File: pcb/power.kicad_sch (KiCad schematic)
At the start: 19 parts, among them CN3 ZX-PH2.0-WT2P, J3 GT-USB-7010ASV, Q1 DMG3415U-7, U2 RT9080-33GJ5, U3 MAX17048G+T10, U4 MCP73831-2DCI/MC

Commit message: Lots of work on schematics
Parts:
- added D2: ESDA7P60-1U1M, prop-devboard:D1610-RD, symbol prop-devboard:ESDA7P60-1U1M
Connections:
- net GND: now also D2.2
- net VBUS: now also D2.1
- net VREG_EN: now reaches R4.1, U2.3 (EN)
- net VIN: now reaches C1.2, D1.1, Q1.3, R4.2, U2.1 (VIN)
- net BAT_SCL renamed I2C3_SCL
- net BAT_SDA renamed I2C3_SDA
- no-connect marks 3 -> 10
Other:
- moved on the sheet: C2, R4, U2

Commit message: Mostly finished PCB layout
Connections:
- net GND: now also U4.9 (EP)
- no-connect marks 10 -> 11
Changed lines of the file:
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@@
+	)
+	(junction
+		(at 190.5 129.54)
+		(diameter 0)
+		(color 0 0 0 0)
 	)
 	(junction
@@
 		(at 55.88 52.07)
 	)
+	(no_connect
+		(at 187.96 127)
+	)
 	(wire
 		(pts
@@
 	(wire
 		(pts
+			(xy 190.5 129.54) (xy 203.2 129.54)
+		)
+		(stroke
+			(width 0)
+			(type default)
+		)
+	)
+	(wire
+		(pts
+			(xy 190.5 121.92) (xy 190.5 129.54)
+		)
+		(stroke
+			(width 0)
+			(type default)
+		)
+	)
+	(wire
+		(pts
 			(xy 165.1 78.74) (xy 171.45 78.74)
 		)
@@
 	(wire
 		(pts
+			(xy 187.96 121.92) (xy 190.5 121.92)
+		)
+		(stroke
+			(width 0)
+			(type default)
+		)
+	)
+	(wire
+		(pts
 			(xy 121.92 135.89) (xy 121.92 140.97)
 		)
@@
 	(wire
 		(pts
-			(xy 187.96 129.54) (xy 203.2 129.54)
-		)
-		(stroke
+			(xy 187.96 129.54) (xy 190.5 129.54)
+		)
+		(stroke

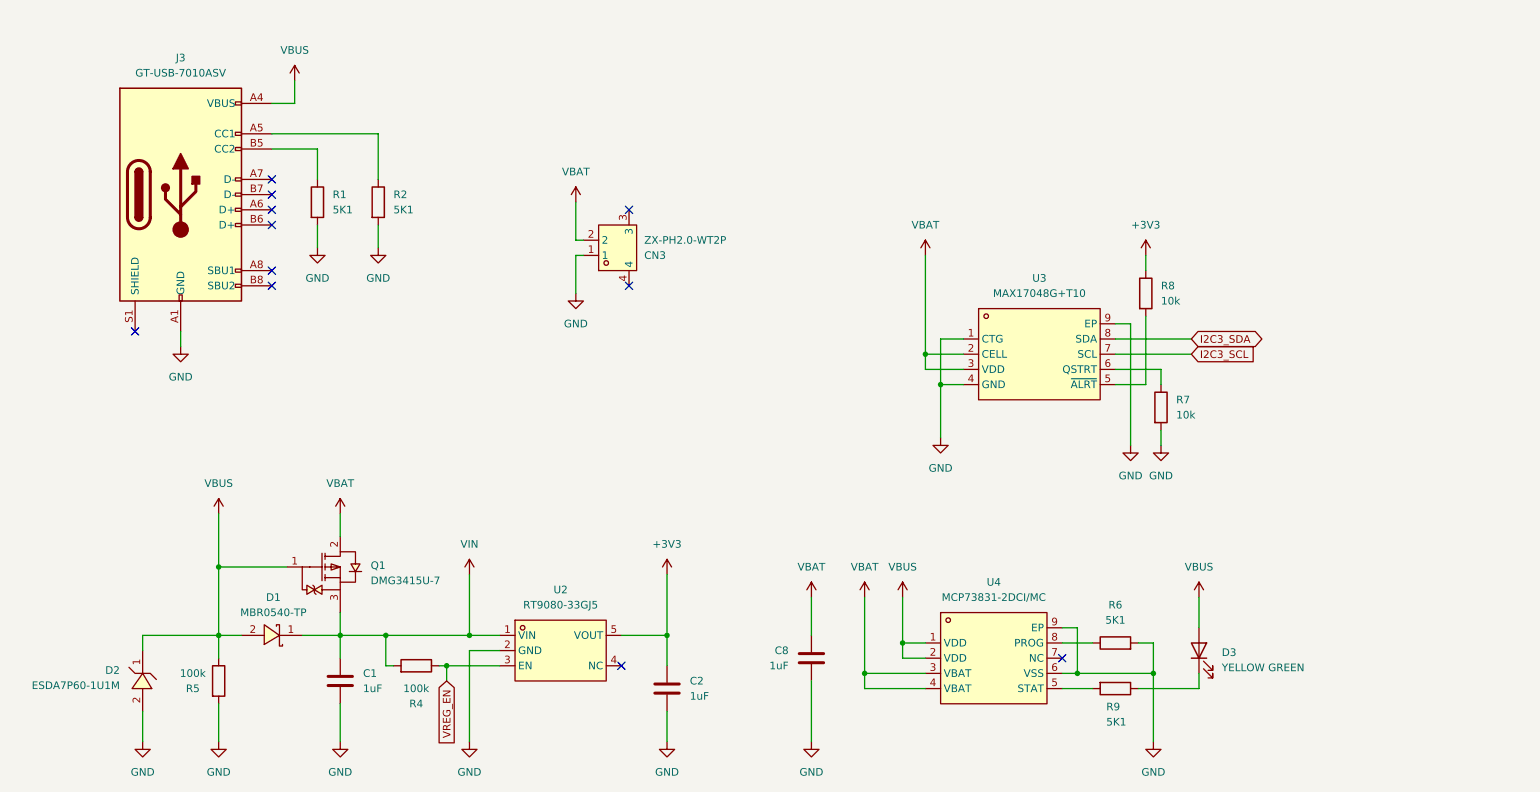
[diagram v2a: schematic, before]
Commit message: Added USB support
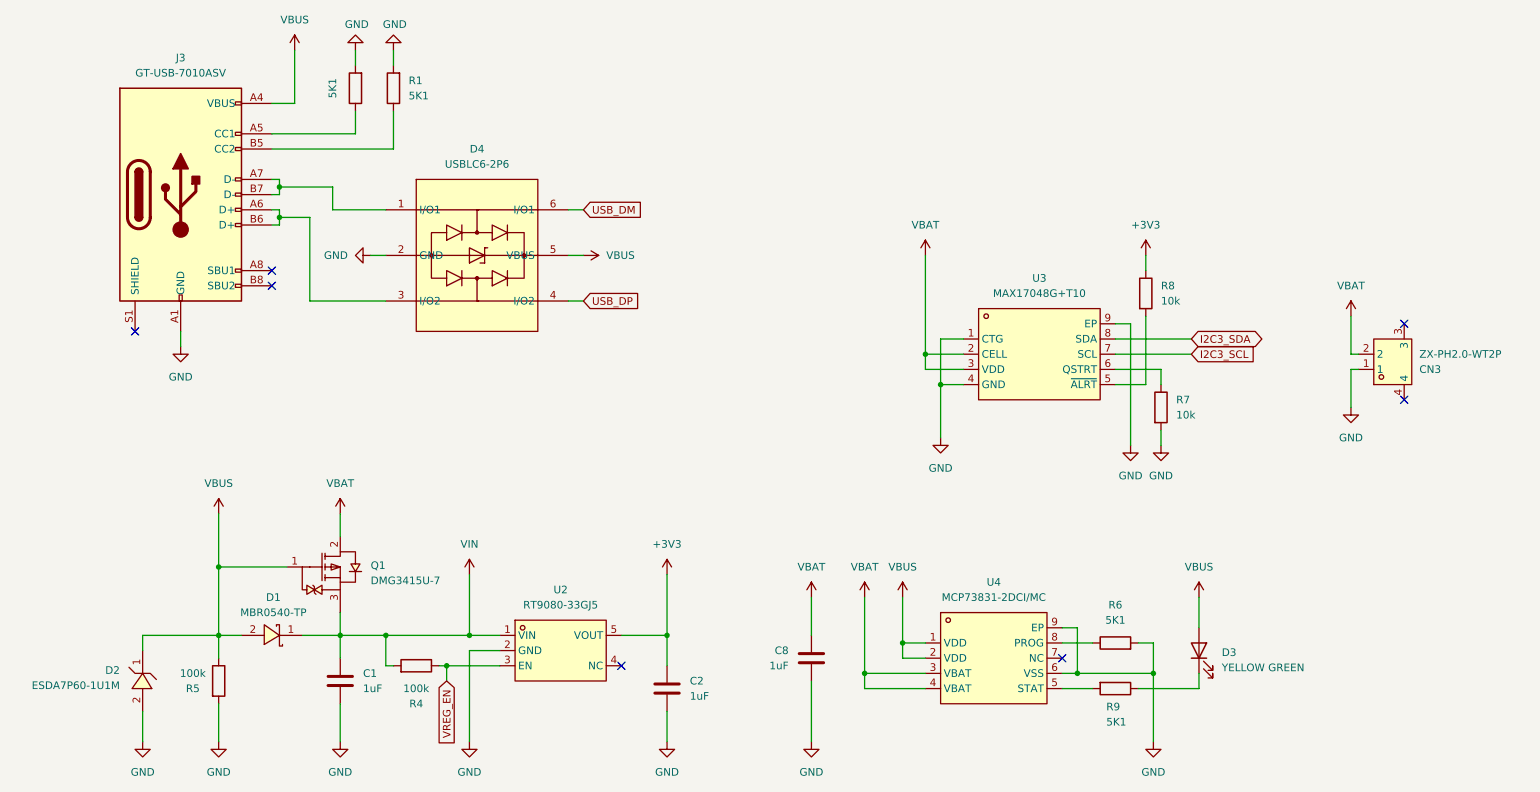
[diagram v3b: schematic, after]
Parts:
- added D4: USBLC6-2P6, prop-devboard:SOT-666-6_L1.6-W1.2-P0.50-LS1.6-BR, symbol prop-devboard:USBLC6-2P6
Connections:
- net GND: now also D4.2 (GND)
- net VBUS: now also D4.5 (VBUS)
- net at J3.A6 (D+): now also J3.B6 (D+), D4.3 (I/O2)
- net at J3.A7 (D-): now also J3.B7 (D-), D4.1 (I/O1)
- new net USB_DM: D4.6 (I/O1)
- new net USB_DP: D4.4 (I/O2)
- no-connect marks 11 -> 7
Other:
- moved on the sheet: CN3, R1

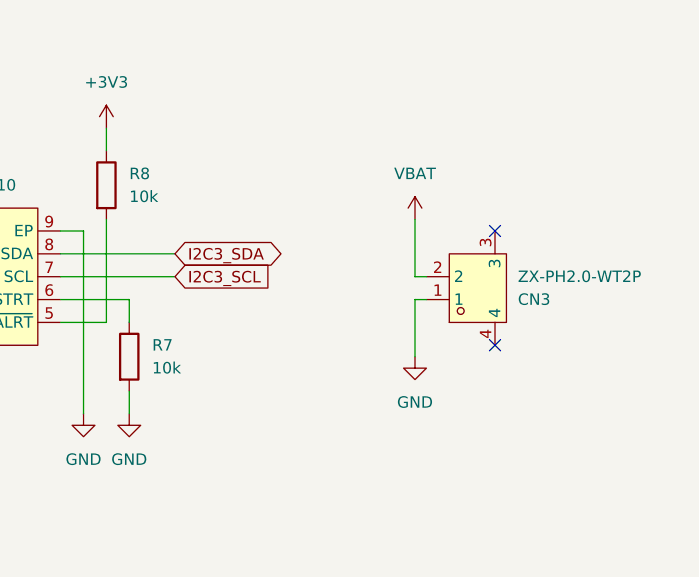
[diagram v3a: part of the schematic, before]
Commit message: Fixed wrong polarity of the battery connector, uffff
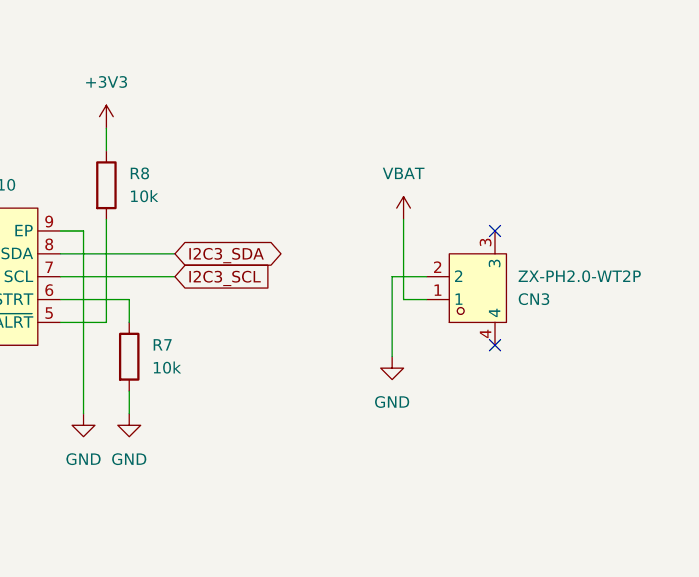
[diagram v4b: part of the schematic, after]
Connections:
- net GND: now also CN3.2; no longer CN3.1
- net VBAT: now also CN3.1; no longer CN3.2
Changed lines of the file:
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@@
 	(wire
 		(pts
-			(xy 236.22 76.2) (xy 236.22 69.85)
-		)
-		(stroke
-			(width 0)
-			(type default)
-		)
-	)
-	(wire
-		(pts
 			(xy 190.5 129.54) (xy 203.2 129.54)
 		)
@@
 	(wire
 		(pts
+			(xy 234.95 69.85) (xy 234.95 78.74)
+		)
+		(stroke
+			(width 0)
+			(type default)
+		)
+	)
+	(wire
+		(pts
 			(xy 88.9 125.73) (xy 88.9 140.97)
 		)
@@
 	(wire
 		(pts
+			(xy 234.95 78.74) (xy 237.49 78.74)
+		)
+		(stroke
+			(width 0)
+			(type default)
+		)
+	)
+	(wire
+		(pts
 			(xy 46.99 111.76) (xy 46.99 123.19)
 		)
@@
 	(wire
 		(pts
-			(xy 237.49 78.74) (xy 236.22 78.74)
-		)
-		(stroke
-			(width 0)
-			(type default)
-		)
-	)
-	(wire
-		(pts
 			(xy 146.05 116.84) (xy 146.05 123.19)
 		)
@@
 	(wire
 		(pts
-			(xy 236.22 78.74) (xy 236.22 85.09)
+			(xy 233.68 76.2) (xy 233.68 85.09)
 		)
 		(stroke
@@
 	(wire
 		(pts
+			(xy 237.49 76.2) (xy 233.68 76.2)
+		)
+		(stroke
+			(width 0)
+			(type default)
+		)
+	)
+	(wire
+		(pts
 			(xy 165.1 76.2) (xy 171.45 76.2)
 		)
@@
 	(wire
 		(pts
-			(xy 237.49 76.2) (xy 236.22 76.2)
-		)
-		(stroke
-			(width 0)
-			(type default)
-		)
-	)
-	(wire
-		(pts
 			(xy 161.29 116.84) (xy 161.29 124.46)
 		)
@@
 	(symbol
 		(lib_id "power:VBUS")
-		(at 236.22 69.85 0)
+		(at 234.95 69.85 0)
 		(unit 1)
 		(exclude_from_sim no)
@@
 		(fields_autoplaced yes)
 		(property "Reference" "#PWR017"
-			(at 236.22 73.66 0)
+			(at 234.95 73.66 0)
 			(effects
 				(font
@@
 		)
 		(property "Value" "VBAT"
-			(at 236.22 64.77 0)
+			(at 234.95 64.77 0)
 			(effects
 				(font
@@
 		)
 		(property "Footprint" ""
-			(at 236.22 69.85 0)
+			(at 234.95 69.85 0)
 			(effects
 				(font
@@
 		)
 		(property "Datasheet" ""
-			(at 236.22 69.85 0)
+			(at 234.95 69.85 0)
 			(effects
 				(font
@@
 		)
 		(property "Description" "Power symbol creates a global label with name \"VBUS\""
-			(at 236.22 69.85 0)
+			(at 234.95 69.85 0)
 			(effects
 				(font
@@
 	(symbol
 		(lib_id "power:GND")
-		(at 236.22 85.09 0)
+		(at 233.68 85.09 0)
 		(unit 1)
 		(exclude_from_sim no)
@@
 		(fields_autoplaced yes)
 		(property "Reference" "#PWR015"
-			(at 236.22 91.44 0)
+			(at 233.68 91.44 0)
 			(effects
 				(font
@@
 		)
 		(property "Value" "GND"
-			(at 236.22 90.17 0)
+			(at 233.68 90.17 0)
 			(effects
 				(font
@@
 		)
 		(property "Footprint" ""
-			(at 236.22 85.09 0)
+			(at 233.68 85.09 0)
 			(effects
 				(font
@@
 		)
 		(property "Datasheet" ""
-			(at 236.22 85.09 0)
+			(at 233.68 85.09 0)
 			(effects
 				(font
@@
 		)
 		(property "Description" "Power symbol creates a global label with name \"GND\" , ground"
-			(at 236.22 85.09 0)
+			(at 233.68 85.09 0)
 			(effects
 				(font

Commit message: Switched battery and QWIIC connectors to black ones, and fixed their positioning to not obstruct bolt heads when M2.5 cylindrical bolts are used to mount the board
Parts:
- CN3: footprint prop-devboard:CONN-SMD_ZX-PH2.0-WT2P -> prop-devboard:CONN-SMD_PH-2AWT; LCSC Part C7429689 -> C19633668
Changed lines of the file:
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@@
 			)
 		)
-		(property "Footprint" "prop-devboard:CONN-SMD_ZX-PH2.0-WT2P"
+		(property "Footprint" "prop-devboard:CONN-SMD_PH-2AWT"
 			(at 241.3 63.5 0)
 			(effects
@@
 			)
 		)
-		(property "LCSC Part" "C7429689"
+		(property "LCSC Part" "C19633668"
 			(at 241.3 60.96 0)
 			(effects
 				(font
+					(size 1.27 1.27)
+				)
+				(hide yes)
+			)
+		)
+		(property "LCSC Part #" ""
+			(at 241.3 77.47 0)
+			(effects
+				(font

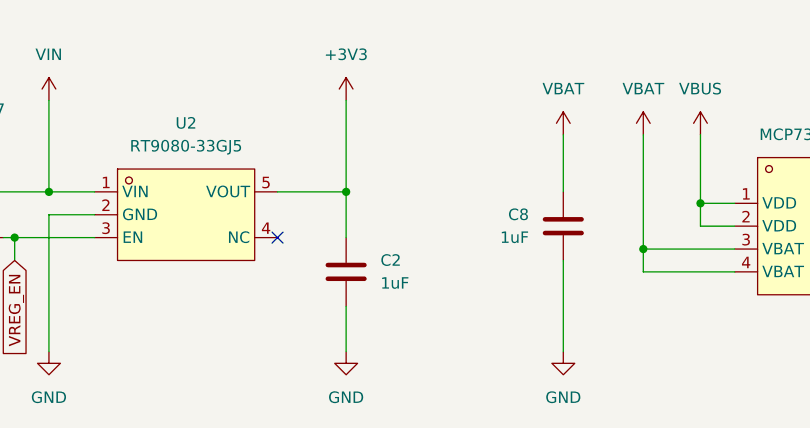
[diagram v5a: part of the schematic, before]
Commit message: Added I2C pull ups, extra bypass capacitance for the MCU and increased the LDO output capacitance
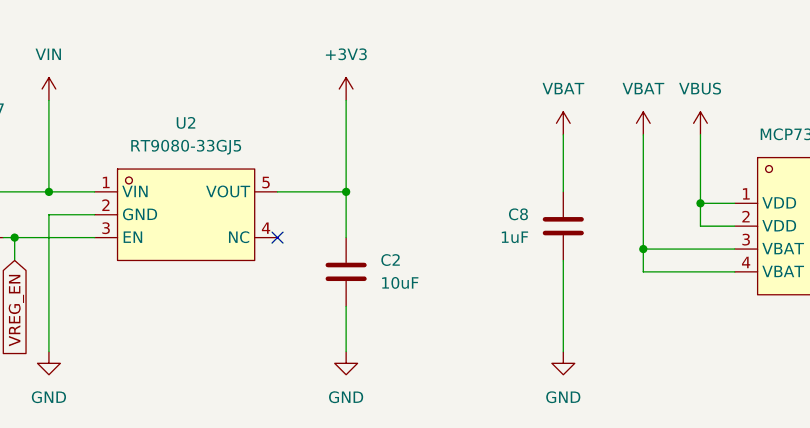
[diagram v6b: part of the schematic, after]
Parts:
- C2: value 1uF -> 10uF; LCSC Part # C14445 -> C15525
- R5: LCSC Part # C60491 -> C25741
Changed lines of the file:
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@@
 			)
 		)
-		(property "Value" "1uF"
+		(property "Value" "10uF"
 			(at 125.73 133.3499 0)
 			(effects
@@
 			)
 		)
-		(property "LCSC Part #" "C14445"
+		(property "LCSC Part #" "C15525"
 			(at 121.92 132.08 0)
 			(effects
@@
 			)
 		)
-		(property "LCSC Part #" "C60491"
+		(property "LCSC Part #" "C25741"
 			(at 46.99 130.81 0)
 			(effects

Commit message: More PCB layout updates
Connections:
- net USBC_DP: now reaches D4.3 (I/O2), J3.A6 (D+), J3.B6 (D+)
- net USBC_DN: now reaches D4.1 (I/O1), J3.A7 (D-), J3.B7 (D-)
- net USB_DM renamed USB_DN
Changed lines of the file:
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@@
+	(wire
+		(pts
+			(xy 62.23 67.31) (xy 74.93 67.31)
+		)
+		(stroke
+			(width 0)
+			(type default)
+		)
+	)
 	(wire
 		(pts
@@
 	(wire
 		(pts
-			(xy 62.23 67.31) (xy 74.93 67.31)
-		)
-		(stroke
-			(width 0)
-			(type default)
-		)
-	)
-	(wire
-		(pts
 			(xy 201.93 69.85) (xy 201.93 81.28)
 		)
@@
 			(width 0)
 			(type default)
+		)
+	)
+	(label "USBC_DN"
+		(at 67.31 52.07 0)
+		(effects
+			(font
+				(size 1.27 1.27)
+			)
+			(justify left bottom)
+		)
+	)
+	(label "USBC_DP"
+		(at 67.31 67.31 0)
+		(effects
+			(font
+				(size 1.27 1.27)
+			)
+			(justify left bottom)
 		)
 	)
@@
 		)
 	)
-	(global_label "USB_DM"
+	(global_label "USB_DN"
 		(shape input)
 		(at 107.95 52.07 0)
@@
 		)
 		(property "Intersheetrefs" "${INTERSHEET_REFS}"
-			(at 118.4342 52.07 0)
+			(at 118.3133 52.07 0)
 			(effects
 				(font
